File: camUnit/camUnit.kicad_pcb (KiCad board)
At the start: 2 copper layers, 87 x 87 mm, 0 parts

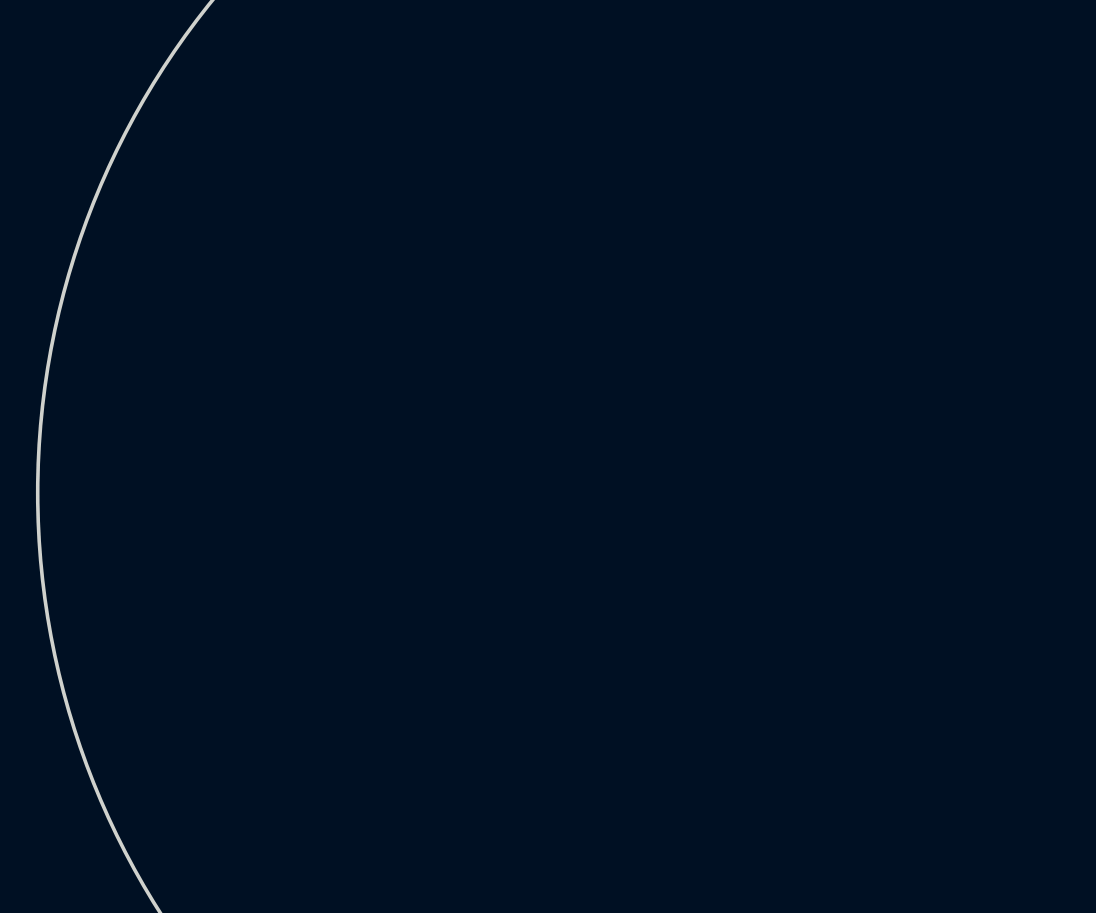
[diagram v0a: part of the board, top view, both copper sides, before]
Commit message: m1n footprint
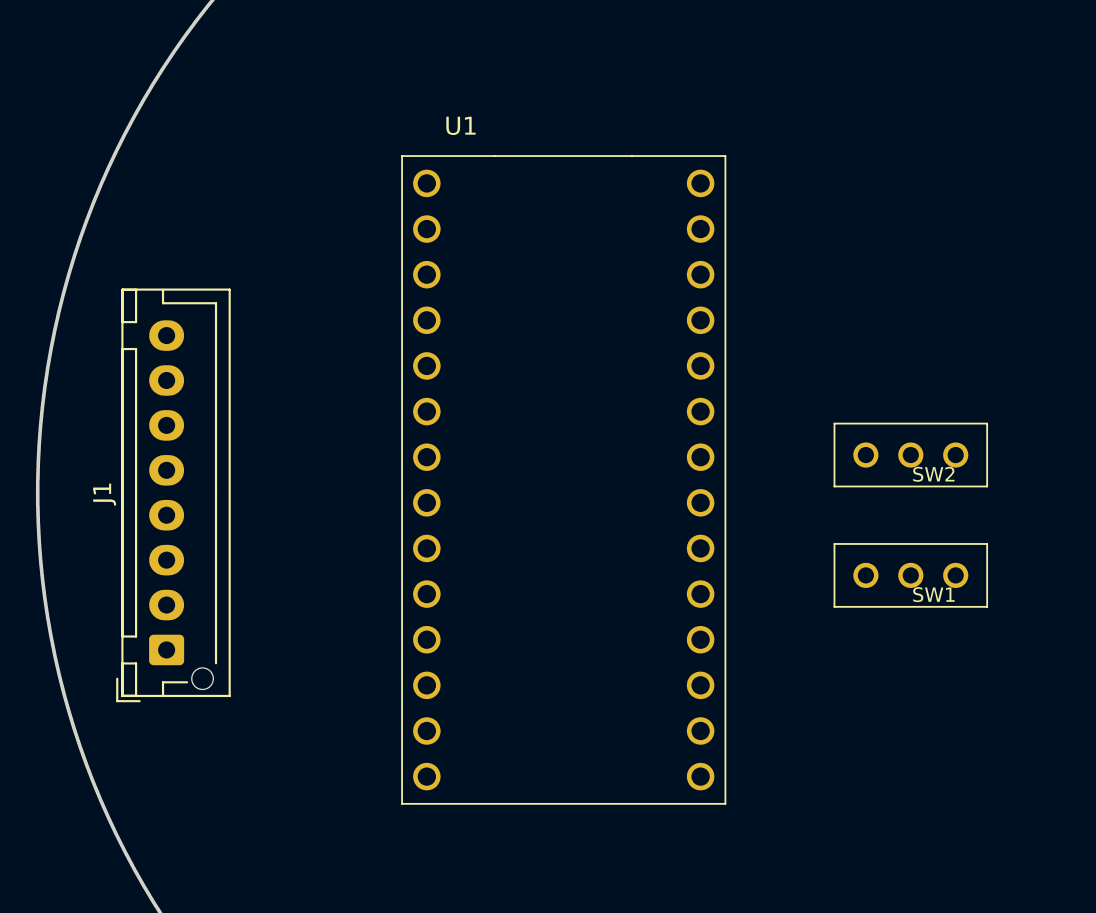
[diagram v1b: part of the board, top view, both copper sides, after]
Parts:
- added J1: Conn_01x08, Connector_JST:JST_XH_B8B-XH-AM_1x08_P2.50mm_Vertical, F.Cu at (100.9, 110.1)
- added SW1: SW_SPDT, Library:SS12D00G3, F.Cu at (142.3, 106.0)
- added SW2: SW_SPDT, Library:SS12D00G3, F.Cu at (142.3, 99.3)
- added U1: Teensy 4.0, Library:Teensy 4.0, F.Cu at (123.0, 100.7)

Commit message: Camunit
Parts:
- added REF**: m1n, Library:m1n, F.Cu at (137.6, 142.8)
- added REF**1: m1n, Library:m1n, F.Cu at (178.6, 101.0)
- added REF**2: m1n, Library:m1n, F.Cu at (136.8, 60.0)
- added REF**3: m1n, Library:m1n, F.Cu at (95.8, 101.8)
- J1: moved to B.Cu
- moved SW2 34.5 mm to (167.6, 122.8)
- moved U1 14.2 mm to (137.2, 101.0), turned to -135 degrees
- moved SW1 13.5 mm to (139.4, 119.2), turned to 135 degrees
- moved J1 12.2 mm to (113.1, 110.9)
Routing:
- added copper zone on B.Cu, net GNDREF
- added copper zone on F.Cu, net GNDREF
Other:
- board size 87 x 87 mm -> 120 x 120 mm

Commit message: Cam Layer
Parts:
- removed REF**, REF**1, REF**2, REF**3: m1n, Library:m1n
- added C1: 2u2, Library:cap0603, F.Cu at (131.0, 106.9)
- added C2: 0u1, Library:cap0603, F.Cu at (143.4, 97.9)
- added C3: 0u1, Library:cap0603, F.Cu at (131.0, 104.7)
- added C4: 0u1, Library:cap0603, F.Cu at (140.4, 107.7)
- added C5: 0u1, Library:cap0603, F.Cu at (140.2, 95.3)
- added C6: 0u1, Library:cap0603, F.Cu at (135.4, 95.3)
- added C7: C, Library:cap0603, F.Cu at (131.6, 86.9)
- added D1: RED, Library:led0603, F.Cu at (143.4, 103.9)
- added J2: Conn_01x04, Connector_PinHeader_2.54mm:PinHeader_1x04_P2.54mm_Vertical, F.Cu at (133.4, 80.0)
- added J3: Conn_01x06, Connector_JST:JST_PH_B6B-PH-K_1x06_P2.00mm_Vertical, F.Cu at (132.2, 60.8)
- added J4: Conn_01x06, Connector_JST:JST_PH_B6B-PH-K_1x06_P2.00mm_Vertical, F.Cu at (96.6, 106.4)
- added J5: Conn_01x06, Connector_JST:JST_PH_B6B-PH-K_1x06_P2.00mm_Vertical, F.Cu at (142.2, 141.9)
- added J6: Conn_01x06, Connector_JST:JST_PH_B6B-PH-K_1x06_P2.00mm_Vertical, F.Cu at (177.7, 96.4)
- added R1: R, Library:res0603, F.Cu at (143.4, 100.3)
- added R2: 1K, Library:res0603, F.Cu at (144.2, 106.8)
- added R3: 1k, Library:res0603, F.Cu at (147.3, 102.5)
- added R4: 1k, Library:res0603, F.Cu at (147.3, 100.3)
- added SW3: SW_SPDT, Library:SS12D00G3, F.Cu at (161.6, 133.4)
- added U2: STM32F103Cx, Package_DFN_QFN:QFN-48-1EP_7x7mm_P0.5mm_EP5.6x5.6mm, F.Cu at (137.2, 101.4)
- added Y1: 8Mhz, Crystal:Resonator_SMD_Murata_CSTxExxV-3Pin_3.0x1.1mm, F.Cu at (137.4, 91.8)
- SW2: value SW_SPDT -> ENC RST; footprint Library:SS12D00G3 -> Button_Switch_THT:SW_PUSH_6mm
- U1: value Teensy 4.0 -> ~; footprint Library:Teensy 4.0 -> Library:OpenMV_RT
- moved SW2 50.9 mm to (134.3, 84.3)
- moved J1 26.6 mm to (86.5, 110.1)
- moved SW1 23.2 mm to (157.7, 133.4), turned to 90 degrees
- moved U1 0.37 mm to (137.2, 101.4), turned to 0 degrees
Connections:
- net /TNSY/CAM3 TX renamed /CAM RST
- J1 pad 1: unconnected-(J1-Pin_1-Pad1) -> GNDREF
- J1 pad 2: unconnected-(J1-Pin_2-Pad2) -> GNDREF
- J1 pad 3: unconnected-(J1-Pin_3-Pad3) -> TOF TX
- J1 pad 4: unconnected-(J1-Pin_4-Pad4) -> TOF RX
- J1 pad 5: unconnected-(J1-Pin_5-Pad5) -> CAM RX
- J1 pad 6: unconnected-(J1-Pin_6-Pad6) -> CAM TX
- J1 pad 7: unconnected-(J1-Pin_7-Pad7) -> +3V3 FILT
- J1 pad 8: unconnected-(J1-Pin_8-Pad8) -> +5V FILT
- SW1 pad 2: /TNSY/TNSY PWR -> /CAM PWR
- SW2 pad 1: +5V FILT -> GNDREF
- SW2 pad 2: /CAM PWR -> /TOF/ENC RST
- U1 pad 0: L3 RX -> unconnected-(U1-P0-MOSI/PWM-Pad0)
- U1 pad 1: L3 TX -> unconnected-(U1-P0-ETH_LED-Pad1)
- U1 pad 10: unconnected-(U1-Pad10) -> CAM RX
- U1 pad 14: /TNSY/CAM2 TX -> unconnected-(U1-3V3_(1A-MAX)-Pad14)
- U1 pad 15: /TNSY/CAM2 RX -> GNDREF
- U1 pad 16: /TNSY/CAM3 RX -> unconnected-(U1-NC-Pad16)
- U1 pad 20: /TNSY/CAM4 TX -> unconnected-(U1-NC-Pad20)
- U1 pad 21: /TNSY/CAM4 RX -> unconnected-(U1-P10-PWM-Pad21)
- U1 pad 7: /TNSY/CAM1 RX -> unconnected-(U1-P3-ETH_TXN-Pad7)
- U1 pad 8: /TNSY/CAM1 TX -> CAM TX
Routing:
- net /TOF/TOF PWR: track 0.00 -> 250.5 mm
- net /TOF/TOF SDA: track 0.00 -> 197.9 mm, vias 0 -> 1
- net /TOF/TOF SCL: track 0.00 -> 186.9 mm
- net +3V3 FILT: track 0.00 -> 141.9 mm, vias 0 -> 5
- net +5V FILT: track 0.00 -> 120.2 mm
- net TOF RX: track 0.00 -> 71.4 mm, vias 0 -> 2
- net TOF TX: track 0.00 -> 68.1 mm, vias 0 -> 2
- net CAM TX: track 0.00 -> 56.2 mm
- net CAM RX: track 0.00 -> 55.6 mm
- net /TOF/TOF3: track 0.00 -> 51.5 mm, vias 0 -> 2
- net /TOF/TOF1: track 0.00 -> 44.1 mm, vias 0 -> 1
- net /TOF/TOF4: track 0.00 -> 43.0 mm, vias 0 -> 2
- net /TOF/TOF2: track 0.00 -> 39.1 mm
- net /TOF/TOF SWDIO: track 0.00 -> 36.7 mm, vias 0 -> 1
- net /TOF/TOF SWCLK: track 0.00 -> 35.2 mm, vias 0 -> 1
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
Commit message: CamUnit
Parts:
- added H1: MountingHole, MountingHole:MountingHole_3.2mm_M3_Pad_Via, F.Cu at (99.1, 70.2)
- added H2: MountingHole, MountingHole:MountingHole_3.2mm_M3_Pad_Via, F.Cu at (175.3, 70.2)
- added H3: MountingHole, MountingHole:MountingHole_3.2mm_M3_Pad_Via, F.Cu at (175.3, 132.6)
- added H4: MountingHole, MountingHole:MountingHole_3.2mm_M3_Pad_Via, F.Cu at (99.1, 132.6)
- moved R2 0.21 mm to (144.1, 107.0)
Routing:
- net /TOF/ENC BOOT0: track 2.60 -> 1.61 mm
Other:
- board text added: "JLCJLCJLCJLC"
